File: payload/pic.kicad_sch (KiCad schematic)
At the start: 6 parts, among them IC301 PIC16F1503-I_SL, J301 TC2030-MCP-NL-10

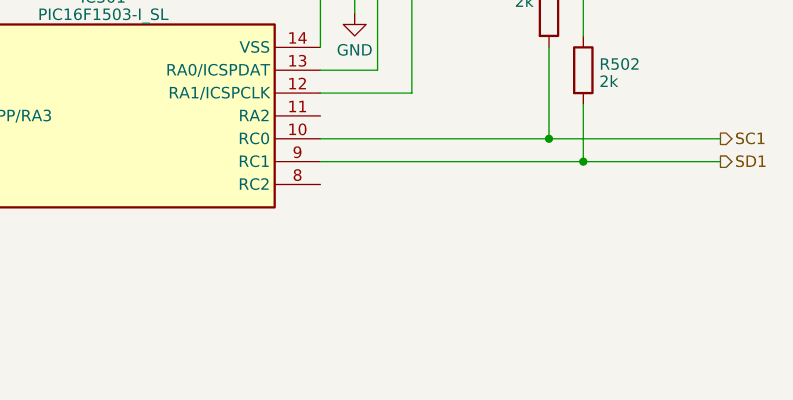
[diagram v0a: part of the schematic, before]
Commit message: added LEDs
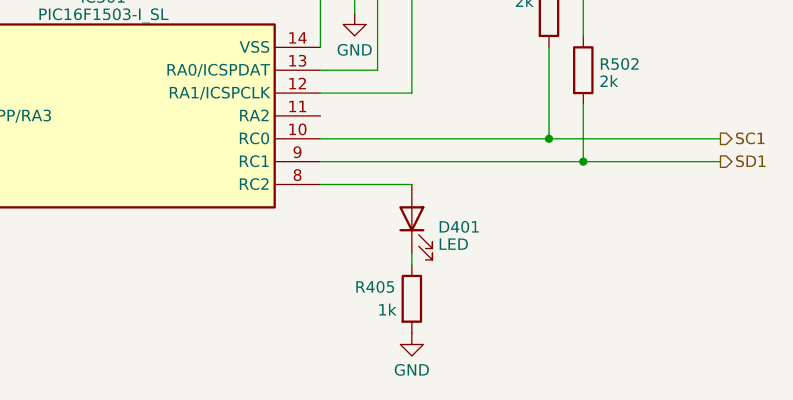
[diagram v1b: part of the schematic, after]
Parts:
- added D401: LED, LED_SMD:LED_0402_1005Metric_Pad0.77x0.64mm_HandSolder, symbol Device:LED
- added R405: 1k, Capacitor_SMD:C_0603_1608Metric_Pad1.08x0.95mm_HandSolder, symbol Device:R
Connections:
- net GND: now also R405.2
- net at IC301.8 (RC2): now also D401.2 (A)
- new net: D401.1 (K), R405.1
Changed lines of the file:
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@@
+    (stroke (width 0) (type default))
+  )
+  (wire (pts (xy 175.26 102.87) (xy 175.26 104.14))
     (stroke (width 0) (type default))
   )
@@
   )
   (wire (pts (xy 106.68 57.15) (xy 106.68 55.88))
+    (stroke (width 0) (type default))
+  )
+  (wire (pts (xy 165.1 95.25) (xy 175.26 95.25))
     (stroke (width 0) (type default))
   )
@@
     )
   )
+  (symbol (lib_id "Device:R") (at 175.26 107.95 0) (unit 1)
+    (in_bom yes) (on_board yes) (dnp no)
+    (property "Reference" "R405" (at 168.91 106.68 0)
+      (effects (font (size 1.27 1.27)) (justify left))
+    )
+    (property "Value" "1k" (at 171.45 109.22 0)
+      (effects (font (size 1.27 1.27)) (justify left))
+    )
+    (property "Footprint" "Capacitor_SMD:C_0603_1608Metric_Pad1.08x0.95mm_HandSolder" (at 173.482 107.95 90)
+      (effects (font (size 1.27 1.27)) hide)
+    )
+    (property "Datasheet" "~" (at 175.26 107.95 0)
+      (effects (font (size 1.27 1.27)) hide)
+    )
+    (pin "1")
+    (pin "2")
+    (instances
+      (project "payload"
+        (path "/0a419cb9-bfa0-442e-8f67-9cc2093d7c87/dea4f99a-06bc-4245-ba10-4d6e21532046"
+          (reference "R405") (unit 1)
+        )
+        (path "/0a419cb9-bfa0-442e-8f67-9cc2093d7c87"
+          (reference "R101") (unit 1)
+        )
+        (path "/0a419cb9-bfa0-442e-8f67-9cc2093d7c87/2a941f93-5df7-46e7-ad12-18d150940b0a"
+          (reference "R201") (unit 1)
+        )
+      )
+      (project "electrical-power-system"
+        (path "/5987de0a-a772-40e3-9e89-af52950d87bb/a29c39c3-f61d-41a4-b663-9cd24fc958f0"
+          (reference "R401") (unit 1)
+        )
+      )
+    )
+  )
   (symbol (lib_id "Device:R") (at 190.5 76.2 0) (unit 1)
     (in_bom yes) (on_board yes) (dnp no)
@@
     )
   )
+  (symbol (lib_id "Device:LED") (at 175.26 99.06 90) (unit 1)
+    (in_bom yes) (on_board yes) (dnp no) (fields_autoplaced)
+    (property "Reference" "D401" (at 178.181 100.0038 90)
+      (effects (font (size 1.27 1.27)) (justify right))
+    )
+    (property "Value" "LED" (at 178.181 101.9248 90)
+      (effects (font (size 1.27 1.27)) (justify right))
+    )
+    (property "Footprint" "LED_SMD:LED_0402_1005Metric_Pad0.77x0.64mm_HandSolder" (at 175.26 99.06 0)
+      (effects (font (size 1.27 1.27)) hide)
+    )
+    (property "Datasheet" "~" (at 175.26 99.06 0)
+      (effects (font (size 1.27 1.27)) hide)
+    )
+    (pin "1")
+    (pin "2")
+    (instances
+      (project "payload"
+        (path "/0a419cb9-bfa0-442e-8f67-9cc2093d7c87/dea4f99a-06bc-4245-ba10-4d6e21532046"
+          (reference "D401") (unit 1)
+        )
+        (path "/0a419cb9-bfa0-442e-8f67-9cc2093d7c87/2a941f93-5df7-46e7-ad12-18d150940b0a"
+          (reference "D201") (unit 1)
+        )
+      )
+    )
+  )
   (symbol (lib_id "Device:R") (at 194.31 82.55 0) (unit 1)
     (in_bom yes) (on_board yes) (dnp no) (fields_autoplaced)
@@
         )
       )
+    )
+  )
+  (symbol (lib_id "power:GND") (at 175.26 111.76 0) (unit 1)
+    (in_bom yes) (on_board yes) (dnp no) (fields_autoplaced)
+    (property "Reference" "#PWR0416" (at 175.26 118.11 0)
+      (effects (font (size 1.27 1.27)) hide)
+    )
+    (property "Value" "GND" (at 175.26 115.8955 0)
+      (effects (font (size 1.27 1.27)))
+    )
+    (property "Footprint" "" (at 175.26 111.76 0)
+      (effects (font (size 1.27 1.27)) hide)
+    )
+    (property "Datasheet" "" (at 175.26 111.76 0)
+      (effects (font (size 1.27 1.27)) hide)
+    )
+    (pin "1")
+    (instances
+      (project "payload"
+        (path "/0a419cb9-bfa0-442e-8f67-9cc2093d7c87/dea4f99a-06bc-4245-ba10-4d6e21532046"
+          (reference "#PWR0416") (unit 1)
+        )
+        (path "/0a419cb9-bfa0-442e-8f67-9cc2093d7c87/2a941f93-5df7-46e7-ad12-18d150940b0a"
+          (reference "#PWR0201") (unit 1)
+        )
+      )
+      (project "electrical-power-system"
+        (path "/5987de0a-a772-40e3-9e89-af52950d87bb/a29c39c3-f61d-41a4-b663-9cd24fc958f0"
+          (reference "#PWR0408") (unit 1)
+        )
+      )
